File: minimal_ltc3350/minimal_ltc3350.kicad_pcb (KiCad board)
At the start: 4 copper layers, 50.8 x 25.4 mm, 43 parts, among them Q1 20.0 V, Q2 20.0 V, Q3 20 V, Q4 20 V, U1 LTC3350EUHF-PBF

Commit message: Add C19 capacitor and update component positions in KiCad project
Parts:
- added C16: 22 µF, capacitor_footprints:C_0805_2012Metric, F.Cu at (161.2, 95.2)
- added C17: 22 µF, capacitor_footprints:C_0805_2012Metric, F.Cu at (157.9, 95.2)
- added C18: 22 µF, capacitor_footprints:C_0805_2012Metric, F.Cu at (161.2, 99.1)
- added C19: 22 µF, capacitor_footprints:C_0805_2012Metric, F.Cu at (157.9, 99.1)

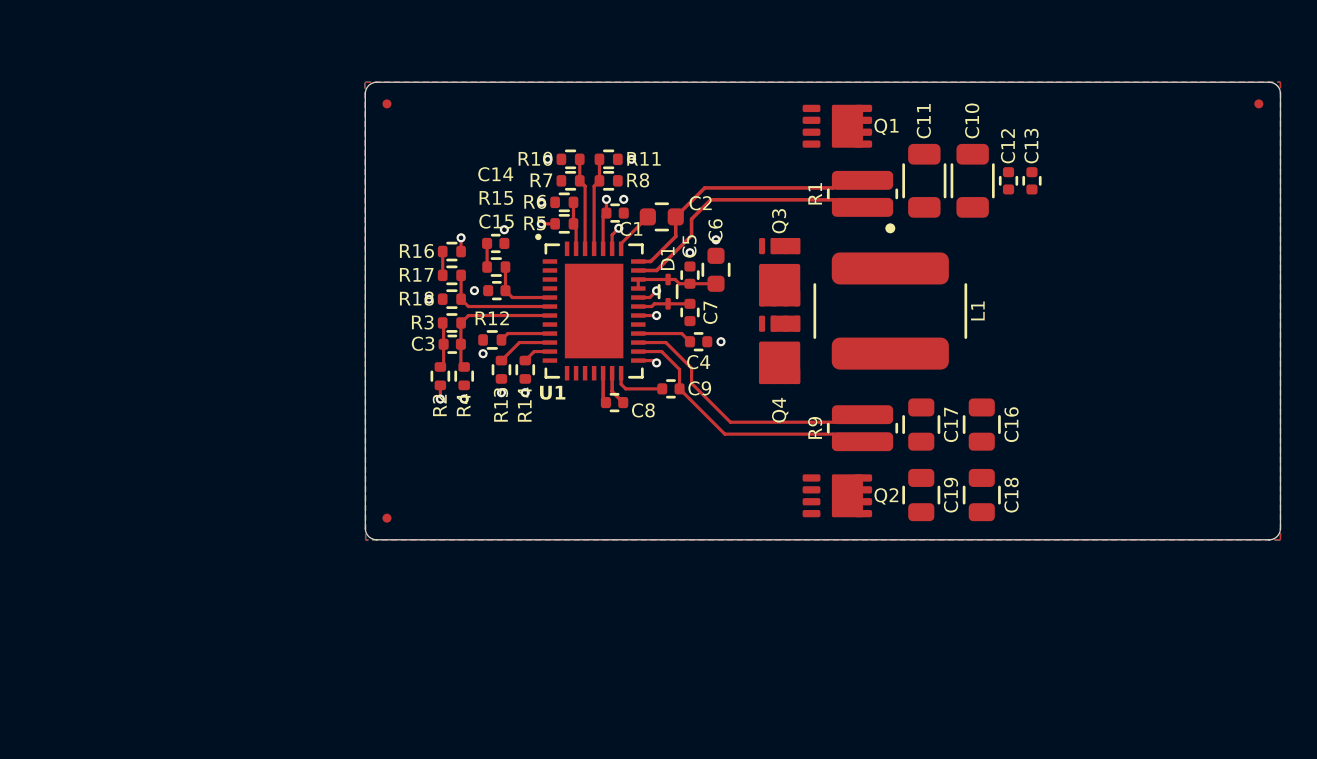
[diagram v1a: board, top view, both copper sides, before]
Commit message: Update component positions and adjust properties in KiCad PCB design
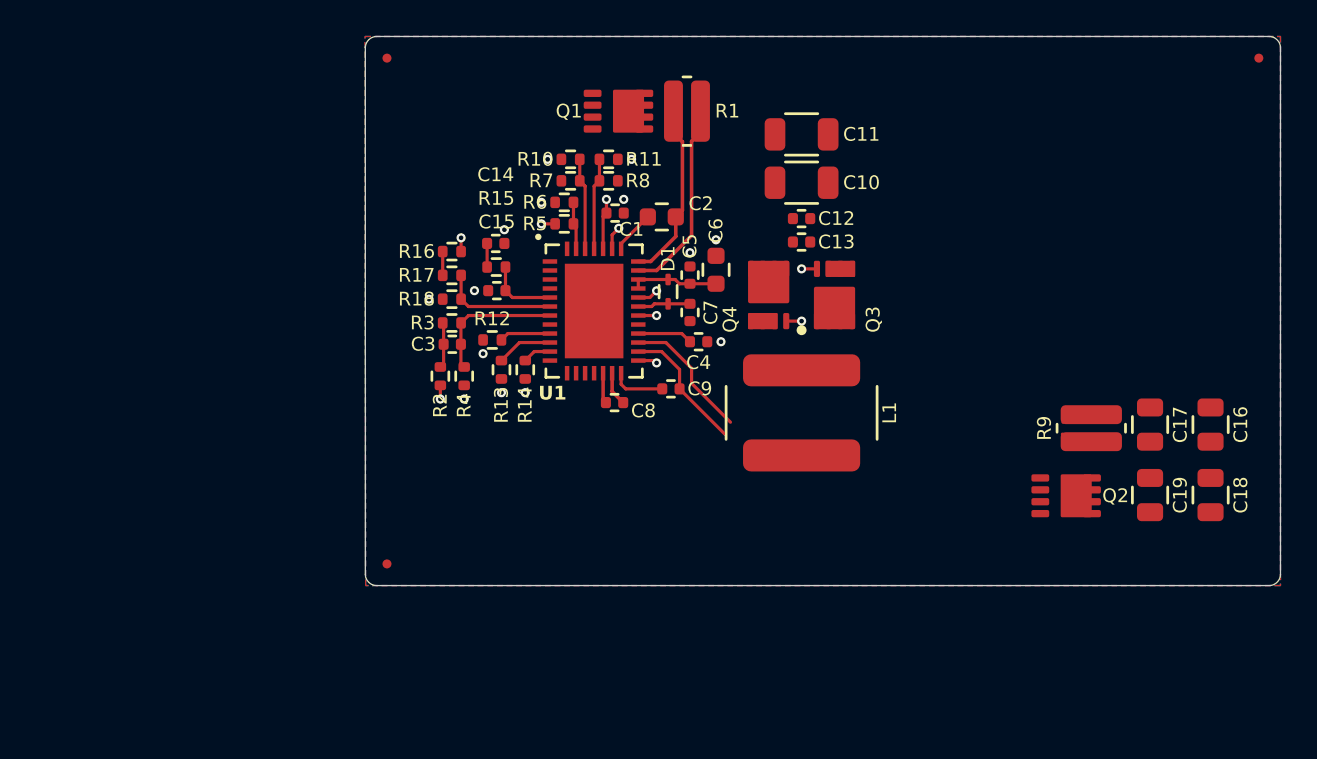
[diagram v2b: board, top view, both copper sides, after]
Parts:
- moved C13 13.2 mm to (151.2, 85.1), turned to 0 degrees
- moved C17 12.7 mm to (170.6, 95.2)
- moved C19 12.7 mm to (170.6, 99.1)
- moved C16 12.7 mm to (173.9, 95.2)
- moved C18 12.7 mm to (173.9, 99.1)
- moved Q2 12.7 mm to (165.9, 99.2)
- moved R9 12.7 mm to (167.3, 95.4)
- moved Q1 12.2 mm to (141.1, 77.8)
- moved C12 11.7 mm to (151.2, 83.8), turned to 0 degrees
- moved R1 10.8 mm to (144.9, 77.8), turned to 0 degrees
- moved C10 9.50 mm to (151.2, 81.8), turned to 0 degrees
- moved L1 7.50 mm to (151.2, 94.6)
- moved C11 7.29 mm to (151.2, 79.1), turned to 0 degrees
- moved Q3 3.30 mm to (153.0, 88.0)
- moved Q4 3.10 mm to (149.4, 88.0), turned to 90 degrees
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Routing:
- net /VCAP: track 15.9 -> 9.87 mm
- net /ICAP: track 14.9 -> 9.19 mm
- net /VOUTSP: track 14.9 -> 9.97 mm
- net /VOUT: track 15.5 -> 11.7 mm
- net /BGATE: track 1.33 -> 2.18 mm, vias 1 -> 2
- net /TGATE: track 1.02 -> 1.87 mm, vias 1 -> 2
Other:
- board size 50.8 x 25.4 mm -> 50.8 x 30.5 mm

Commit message: Update KiCAD PCB file
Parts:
- moved C16 26.4 mm to (148.1, 100.9), turned to -90 degrees
- moved R9 22.5 mm to (144.9, 96.9), turned to 180 degrees
- moved Q2 21.2 mm to (144.8, 101.2), turned to 90 degrees
- moved C17 20.9 mm to (150.5, 100.9), turned to -90 degrees
- moved FID3 20.3 mm to (156.3, 74.9)
- moved C18 18.8 mm to (155.2, 100.9)
- moved C19 17.8 mm to (152.8, 100.9)
- moved FID1 2.54 mm to (128.2, 105.5)
- moved Q3 0.25 mm to (153.3, 88.0)
- moved L1 0.13 mm to (151.3, 94.6)
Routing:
- net /VCAP: track 9.87 -> 8.51 mm
- net /ICAP: track 9.19 -> 8.59 mm
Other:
- board size 50.8 x 30.5 mm -> 30.5 x 33 mm

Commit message: Update KiCAD project files and symbols generator
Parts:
- added R19: 2.7 Ω, resistor_footprints:R_0805_2012Metric, F.Cu at (141.4, 98.5)
- added R20: 2.7 Ω, resistor_footprints:R_0805_2012Metric, F.Cu at (139.2, 98.5)
- added R21: 2.7 Ω, resistor_footprints:R_0805_2012Metric, F.Cu at (137.0, 98.5)
- added R22: 2.7 Ω, resistor_footprints:R_0805_2012Metric, F.Cu at (134.9, 98.5)
- added R23: 2.7 Ω, resistor_footprints:R_0805_2012Metric, F.Cu at (134.0, 95.3)
- moved C14 0.66 mm to (133.7, 84.7)
- moved R15 0.55 mm to (133.8, 86.2)
- moved C15 0.51 mm to (133.8, 87.8)
- moved C4 0.36 mm to (145.8, 90.9)
- moved C5 0.33 mm to (145.3, 86.7)
- moved C6 0.33 mm to (146.7, 86.4)
- moved C3 0.25 mm to (131.6, 90.7)
- moved R12 0.25 mm to (133.8, 90.5)
- moved R13 0.25 mm to (134.3, 92.2)
- moved R14 0.25 mm to (135.6, 92.2)
- moved R16 0.25 mm to (131.6, 85.6)
- moved R17 0.25 mm to (131.6, 86.9)
- moved R18 0.25 mm to (131.6, 88.2)
- moved R2 0.25 mm to (130.9, 92.5)
- moved R3 0.25 mm to (131.6, 89.6)
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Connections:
- U1 pad 12: unconnected-(U1-CAPRTN-Pad12) -> /CAPRTN
- U1 pad 13: unconnected-(U1-CAP1-Pad13) -> /CAP1
- U1 pad 14: unconnected-(U1-CAP2-Pad14) -> /CAP2
- U1 pad 15: unconnected-(U1-CAP3-Pad15) -> /CAP3
- U1 pad 16: unconnected-(U1-CAP4-Pad16) -> /CAP4
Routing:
- net /CAP1: track 0.00 -> 6.66 mm
- net /CAP3: track 0.00 -> 6.32 mm
- net /CAP2: track 0.00 -> 5.97 mm
- net /CAP4: track 0.00 -> 5.97 mm
- net /CAPRTN: track 0.00 -> 4.77 mm
- net /INFET: track 1.30 -> 2.31 mm, vias 1 -> 2
- net /OUTFET: track 1.07 -> 2.09 mm, vias 1 -> 2
- net /VC: track 3.94 -> 4.66 mm
- added copper zone on F.Cu, net /SW
- added copper zone on F.Cu, net /VOUT

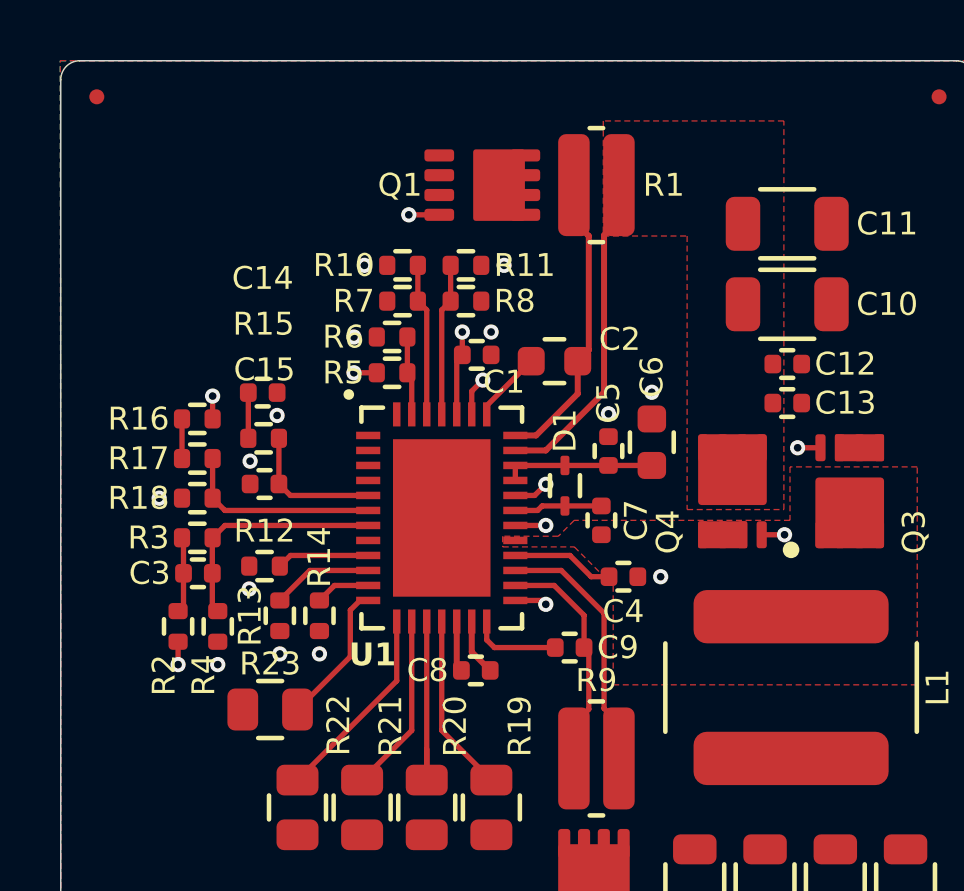
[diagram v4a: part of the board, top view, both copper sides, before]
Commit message: Update KiCad project: Add LED components and adjust resistor positions
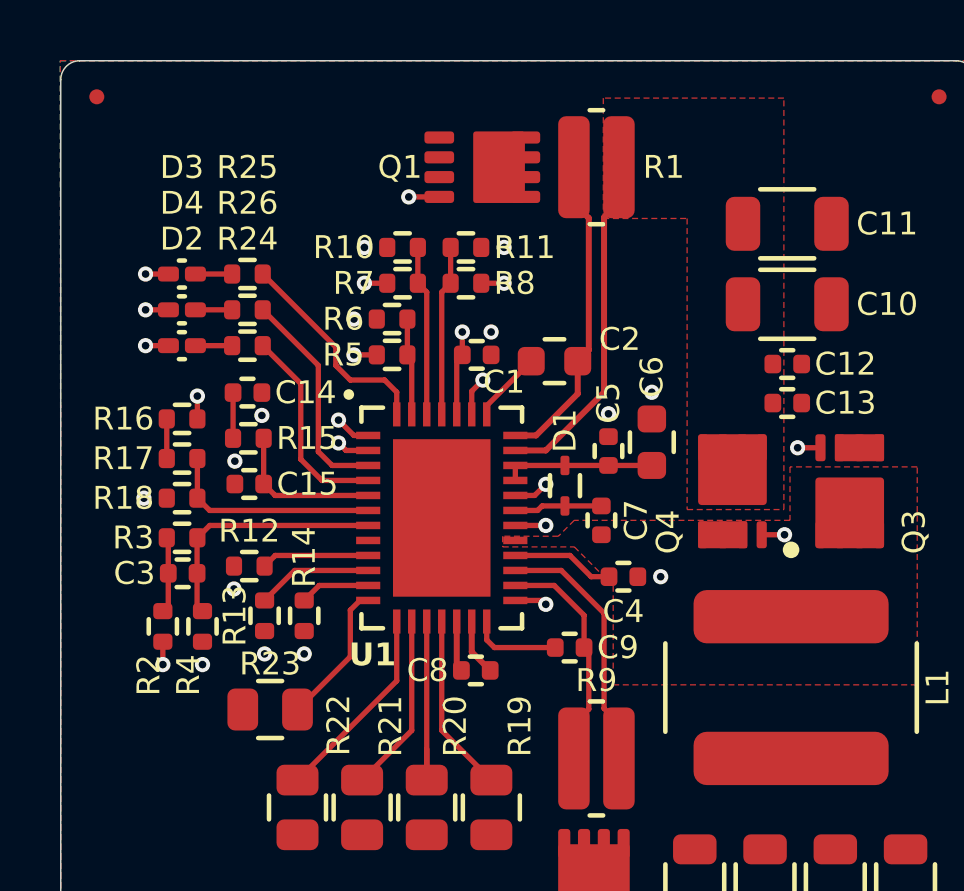
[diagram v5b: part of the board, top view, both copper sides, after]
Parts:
- added D2: 1.8 V, diode_footprints:LED_RED_0402_1005Metric, F.Cu at (131.0, 83.2)
- added D3: 1.8 V, diode_footprints:LED_RED_0402_1005Metric, F.Cu at (131.0, 80.8)
- added D4: 1.8 V, diode_footprints:LED_RED_0402_1005Metric, F.Cu at (131.0, 82.0)
- added R24: 1 kΩ, resistor_footprints:R_0402_1005Metric, F.Cu at (133.2, 83.2)
- added R25: 1 kΩ, resistor_footprints:R_0402_1005Metric, F.Cu at (133.2, 80.8)
- added R26: 1 kΩ, resistor_footprints:R_0402_1005Metric, F.Cu at (133.2, 82.0)
- moved Q1 0.60 mm to (141.1, 77.2)
- moved R1 0.60 mm to (144.9, 77.2)
- moved R10 0.60 mm to (138.4, 79.9)
- moved R11 0.60 mm to (140.5, 79.9)
- moved R5 0.60 mm to (138.0, 83.5)
- moved R7 0.60 mm to (138.4, 81.1)
- moved R8 0.60 mm to (140.5, 81.1)
- moved R6 0.60 mm to (138.0, 82.3)
- moved R13 0.51 mm to (133.8, 92.2)
- moved R14 0.51 mm to (135.1, 92.2)
- moved R16 0.51 mm to (131.0, 85.6)
- moved R17 0.51 mm to (131.0, 86.9)
- moved R18 0.51 mm to (131.0, 88.2)
- moved R3 0.51 mm to (131.0, 89.6)
- moved R4 0.51 mm to (131.7, 92.5)
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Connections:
- U1 pad 3: unconnected-(U1-~{SMBALERT}-Pad3) -> /~{SMBALERT}
- U1 pad 38: unconnected-(U1-~{PFO}-Pad38) -> /~{PFO}
- U1 pad 4: unconnected-(U1-CAPGD-Pad4) -> /CAPGD
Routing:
- net /~{SMBALERT}: track 0.00 -> 7.35 mm
- net /~{PFO}: track 0.00 -> 7.20 mm
- net /CAPGD: track 0.00 -> 6.85 mm
- net /INTVCC: track 5.05 -> 7.34 mm, vias 0 -> 3
- net /VCC2P5: track 3.42 -> 4.94 mm, vias 0 -> 2
- net Net-(D4-Pad1): track 0.00 -> 1.22 mm
- net Net-(D3-Pad1): track 0.00 -> 1.22 mm
- net Net-(D2-Pad1): track 0.00 -> 1.22 mm
- net unconnected-(U1-SCL-Pad1): track 0.00 -> 1.20 mm, vias 0 -> 1
- net unconnected-(U1-SDA-Pad2): track 0.00 -> 1.09 mm, vias 0 -> 1
- net /VOUT: track 11.7 -> 12.3 mm
- net /CAP_SLCT1: track 5.09 -> 5.69 mm
- net /CAP_SLCT0: track 5.09 -> 5.69 mm
- net /VOUTSP: track 9.97 -> 10.6 mm
- net /PFI: track 2.64 -> 3.24 mm
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
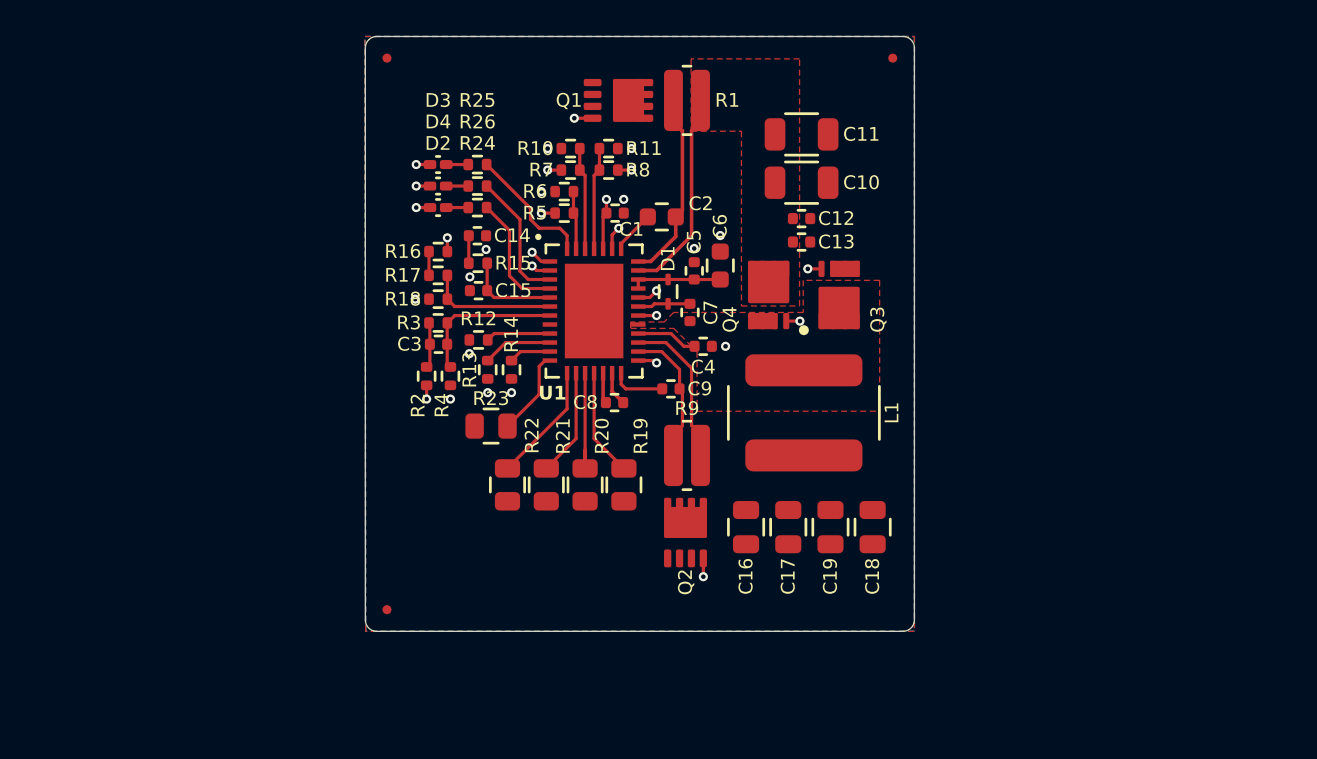
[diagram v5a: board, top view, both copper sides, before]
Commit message: Update KiCad project: Update PCB layout and schematic
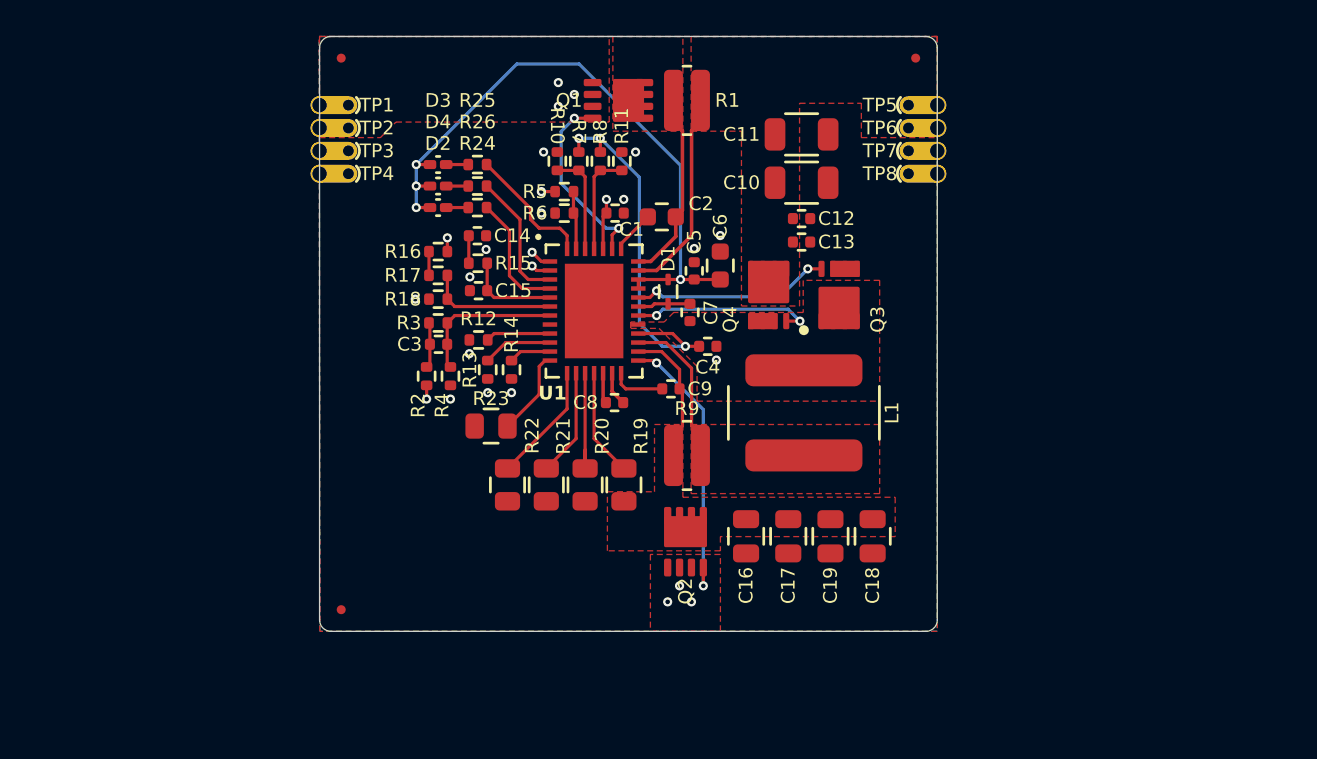
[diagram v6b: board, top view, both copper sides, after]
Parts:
- added TP1: TestPoint, test_point_footprints:TestPoint_THTPad_Castelated, F.Cu at (124.5, 77.5)
- added TP2: TestPoint, test_point_footprints:TestPoint_THTPad_Castelated, F.Cu at (124.5, 78.7)
- added TP3: TestPoint, test_point_footprints:TestPoint_THTPad_Castelated, F.Cu at (124.5, 80.0)
- added TP4: TestPoint, test_point_footprints:TestPoint_THTPad_Castelated, F.Cu at (124.5, 81.3)
- added TP5: TestPoint, test_point_footprints:TestPoint_THTPad_Castelated, F.Cu at (158.7, 77.5)
- added TP6: TestPoint, test_point_footprints:TestPoint_THTPad_Castelated, F.Cu at (158.7, 78.7)
- added TP7: TestPoint, test_point_footprints:TestPoint_THTPad_Castelated, F.Cu at (158.7, 80.0)
- added TP8: TestPoint, test_point_footprints:TestPoint_THTPad_Castelated, F.Cu at (158.7, 81.3)
- moved FID1 2.54 mm to (125.7, 105.5)
- moved FID2 2.54 mm to (125.7, 74.9)
- moved FID3 1.27 mm to (157.5, 74.9)
- moved R5 1.19 mm to (138.0, 82.3)
- moved R6 1.19 mm to (138.0, 83.5)
- moved R10 1.02 mm to (137.7, 80.6), turned to 90 degrees
- moved R11 1.01 mm to (141.2, 80.6), turned to 90 degrees
- moved R8 0.67 mm to (140.0, 80.6), turned to -90 degrees
- moved R7 0.67 mm to (138.9, 80.6), turned to -90 degrees
- moved C16 0.51 mm to (148.1, 101.4)
- moved C17 0.51 mm to (150.5, 101.4)
- moved C18 0.51 mm to (155.2, 101.4)
- moved C19 0.51 mm to (152.8, 101.4)
- moved Q2 0.51 mm to (144.8, 101.7)
- moved C4 0.25 mm to (146.0, 90.9)
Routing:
- net /INTVCC: track 7.34 -> 35.4 mm, vias 3 -> 4
- net /VCC2P5: track 4.94 -> 20.6 mm, vias 2 -> 3
- net /OUTFET: track 2.09 -> 15.5 mm
- net /BGATE: track 2.09 -> 11.3 mm
- net /TGATE: track 1.78 -> 10.2 mm
- net /INFET: track 2.31 -> 10.5 mm
- net /VOUT: vias 1 -> 4
- net /VIN: vias 2 -> 5
- added copper zone on F.Cu, net /ICAP
- added copper zone on F.Cu, net /VCAP
- added copper zone on F.Cu, net /VIN
- added copper zone on In1.Cu, net /VIN
- added copper zone on In1.Cu, net /VOUT
- added copper zone on F.Cu, net /VOUTSP
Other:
- board size 30.5 x 33 mm -> 34.3 x 33 mm

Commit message: Update KiCAD files and symbol table
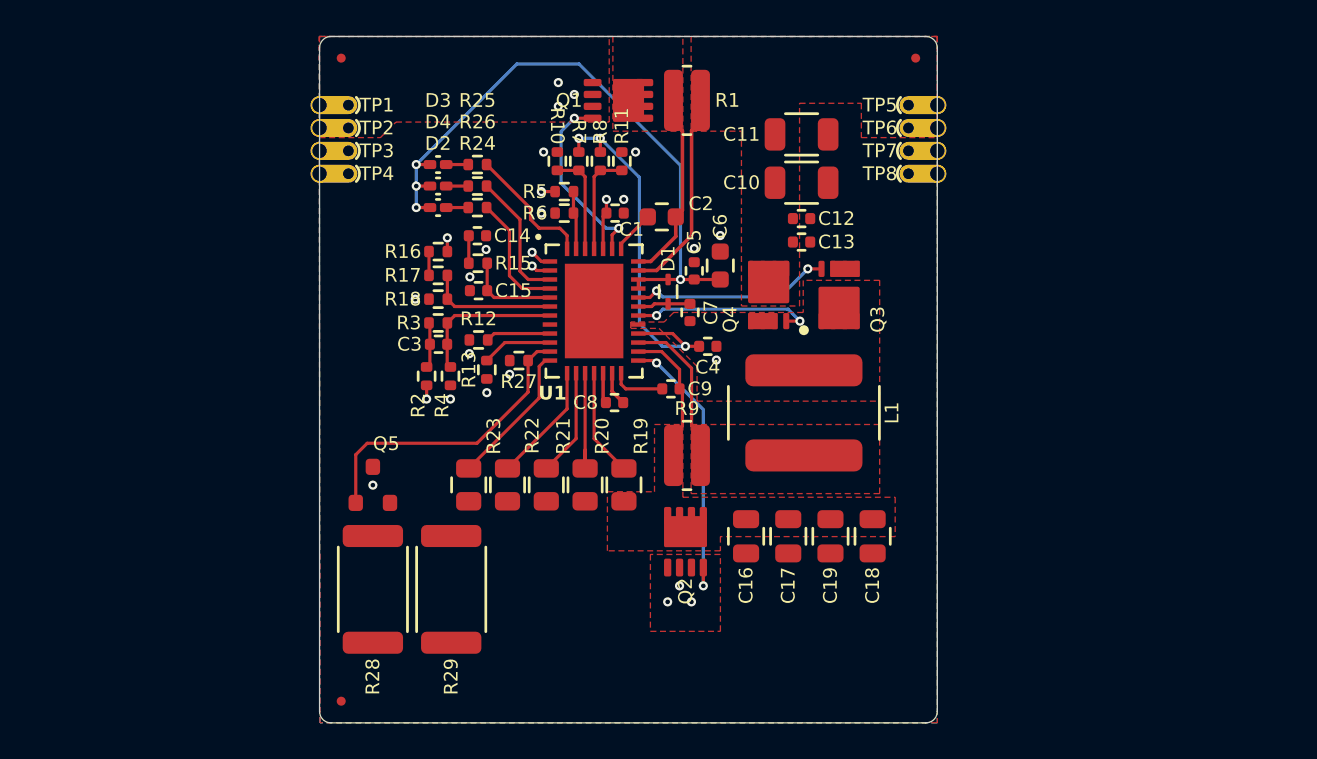
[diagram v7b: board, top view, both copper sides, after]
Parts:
- removed R14: 121 Ω, resistor_footprints:R_0402_1005Metric
- added Q5: 20.0 V, transistor_footprints:SOT23, F.Cu at (127.4, 98.5)
- added R27: 10 MΩ, resistor_footprints:R_0402_1005Metric, F.Cu at (135.5, 91.7)
- added R28: 100 Ω, resistor_footprints:R_2512_6332Metric, F.Cu at (127.4, 104.4)
- added R29: 100 Ω, resistor_footprints:R_2512_6332Metric, F.Cu at (131.8, 104.4)
- moved FID1 5.08 mm to (125.7, 110.6)
- moved R23 3.49 mm to (132.7, 98.5), turned to -90 degrees
- moved R13 0.05 mm to (133.7, 92.2)
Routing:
- net /ITST: track 2.34 -> 16.9 mm
- net /CAPRTN: track 4.77 -> 8.01 mm
- net GND: vias 14 -> 15
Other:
- board size 34.3 x 33 mm -> 34.3 x 38.1 mm
